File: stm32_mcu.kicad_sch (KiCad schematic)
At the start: 6 parts, among them J4 Conn_ARM_SWD_TagConnect_TC203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, U1 STM32G031J6Mx

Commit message: Update polygons
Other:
- moved on the sheet: J4
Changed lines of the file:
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@@
     (stroke (width 0) (type default))
   )
-  (wire (pts (xy 78.74 76.2) (xy 83.82 76.2))
+  (wire (pts (xy 267.97 76.2) (xy 273.05 76.2))
     (stroke (width 0) (type default))
   )
@@
     (stroke (width 0) (type default))
   )
-  (wire (pts (xy 78.74 81.28) (xy 83.82 81.28))
+  (wire (pts (xy 267.97 81.28) (xy 273.05 81.28))
     (stroke (width 0) (type default))
   )
@@
     (stroke (width 0) (type default))
   )
-  (wire (pts (xy 78.74 83.82) (xy 83.82 83.82))
+  (wire (pts (xy 267.97 83.82) (xy 273.05 83.82))
     (stroke (width 0) (type default))
   )
@@
     (stroke (width 0) (type default))
   )
-  (wire (pts (xy 68.58 91.44) (xy 68.58 92.71))
-    (stroke (width 0) (type default))
-  )
-  (wire (pts (xy 68.58 66.04) (xy 68.58 71.12))
+  (wire (pts (xy 257.81 91.44) (xy 257.81 92.71))
+    (stroke (width 0) (type default))
+  )
+  (wire (pts (xy 257.81 66.04) (xy 257.81 71.12))
     (stroke (width 0) (type default))
   )
@@
     )
   )
-  (global_label "JTMS" (shape input) (at 83.82 83.82 0)
-    (effects (font (size 1.27 1.27)) (justify left))
-    (property "Intersheetrefs" "${INTERSHEET_REFS}" (at 90.2334 83.82 0)
+  (global_label "JTMS" (shape input) (at 273.05 83.82 0)
+    (effects (font (size 1.27 1.27)) (justify left))
+    (property "Intersheetrefs" "${INTERSHEET_REFS}" (at 279.4634 83.82 0)
       (effects (font (size 1.27 1.27)) hide)
     )
@@
     )
   )
-  (global_label "JTCK" (shape input) (at 83.82 81.28 0)
-    (effects (font (size 1.27 1.27)) (justify left))
-    (property "Intersheetrefs" "${INTERSHEET_REFS}" (at 90.2334 81.28 0)
+  (global_label "JTCK" (shape input) (at 273.05 81.28 0)
+    (effects (font (size 1.27 1.27)) (justify left))
+    (property "Intersheetrefs" "${INTERSHEET_REFS}" (at 279.4634 81.28 0)
       (effects (font (size 1.27 1.27)) hide)
     )
@@
     )
   )
-  (global_label "JNRST" (shape input) (at 83.82 76.2 0)
-    (effects (font (size 1.27 1.27)) (justify left))
-    (property "Intersheetrefs" "${INTERSHEET_REFS}" (at 90.2334 76.2 0)
+  (global_label "JNRST" (shape input) (at 273.05 76.2 0)
+    (effects (font (size 1.27 1.27)) (justify left))
+    (property "Intersheetrefs" "${INTERSHEET_REFS}" (at 279.4634 76.2 0)
       (effects (font (size 1.27 1.27)) hide)
     )
@@
     )
   )
-  (symbol (lib_id "power:GND") (at 68.58 92.71 0) (unit 1)
-    (in_bom yes) (on_board yes) (dnp no)
-    (property "Reference" "#PWR09" (at 68.58 99.06 0)
-      (effects (font (size 1.27 1.27)) hide)
-    )
-    (property "Value" "GND" (at 68.707 97.1042 0)
-      (effects (font (size 1.27 1.27)))
-    )
-    (property "Footprint" "" (at 68.58 92.71 0)
-      (effects (font (size 1.27 1.27)) hide)
-    )
-    (property "Datasheet" "" (at 68.58 92.71 0)
+  (symbol (lib_id "power:GND") (at 257.81 92.71 0) (unit 1)
+    (in_bom yes) (on_board yes) (dnp no)
+    (property "Reference" "#PWR09" (at 257.81 99.06 0)
+      (effects (font (size 1.27 1.27)) hide)
+    )
+    (property "Value" "GND" (at 257.937 97.1042 0)
+      (effects (font (size 1.27 1.27)))
+    )
+    (property "Footprint" "" (at 257.81 92.71 0)
+      (effects (font (size 1.27 1.27)) hide)
+    )
+    (property "Datasheet" "" (at 257.81 92.71 0)
       (effects (font (size 1.27 1.27)) hide)
     )
@@
     )
   )
-  (symbol (lib_id "power:+5V") (at 68.58 66.04 0) (unit 1)
-    (in_bom yes) (on_board yes) (dnp no)
-    (property "Reference" "#PWR08" (at 68.58 69.85 0)
-      (effects (font (size 1.27 1.27)) hide)
-    )
-    (property "Value" "+5V" (at 68.961 61.6458 0)
-      (effects (font (size 1.27 1.27)))
-    )
-    (property "Footprint" "" (at 68.58 66.04 0)
-      (effects (font (size 1.27 1.27)) hide)
-    )
-    (property "Datasheet" "" (at 68.58 66.04 0)
+  (symbol (lib_id "power:+5V") (at 257.81 66.04 0) (unit 1)
+    (in_bom yes) (on_board yes) (dnp no)
+    (property "Reference" "#PWR08" (at 257.81 69.85 0)
+      (effects (font (size 1.27 1.27)) hide)
+    )
+    (property "Value" "+5V" (at 258.191 61.6458 0)
+      (effects (font (size 1.27 1.27)))
+    )
+    (property "Footprint" "" (at 257.81 66.04 0)
+      (effects (font (size 1.27 1.27)) hide)
+    )
+    (property "Datasheet" "" (at 257.81 66.04 0)
       (effects (font (size 1.27 1.27)) hide)
     )
@@
     )
   )
-  (symbol (lib_id "Connector:Conn_ARM_SWD_TagConnect_TC2030-NL") (at 71.12 81.28 0) (unit 1)
+  (symbol (lib_id "Connector:Conn_ARM_SWD_TagConnect_TC2030-NL") (at 260.35 81.28 0) (unit 1)
     (in_bom no) (on_board yes) (dnp no) (fields_autoplaced)
-    (property "Reference" "J4" (at 64.77 80.01 0)
+    (property "Reference" "J4" (at 254 80.01 0)
       (effects (font (size 1.27 1.27)) (justify right))
     )
-    (property "Value" "Conn_ARM_SWD_TagConnect_TC2030-NL" (at 64.77 82.55 0)
+    (property "Value" "Conn_ARM_SWD_TagConnect_TC2030-NL" (at 254 82.55 0)
       (effects (font (size 1.27 1.27)) (justify right))
     )
-    (property "Footprint" "Connector:Tag-Connect_TC2030-IDC-NL_2x03_P1.27mm_Vertical" (at 71.12 99.06 0)
-      (effects (font (size 1.27 1.27)) hide)
-    )
-    (property "Datasheet" "https://www.tag-connect.com/wp-content/uploads/bsk-pdf-manager/TC2030-CTX_1.pdf" (at 71.12 96.52 0)
-      (effects (font (size 1.27 1.27)) hide)
-    )
+    (property "Footprint" "Connector:Tag-Connect_TC2030-IDC-NL_2x03_P1.27mm_Vertical" (at 260.35 99.06 0)
+      (effects (font (size 1.27 1.27)) hide)
+    )
+    (property "Datasheet" "https://www.tag-connect.com/wp-content/uploads/bsk-pdf-manager/TC2030-CTX_1.pdf" (at 260.35 96.52 0)
+      (effects (font (size 1.27 1.27)) hide)
+    )

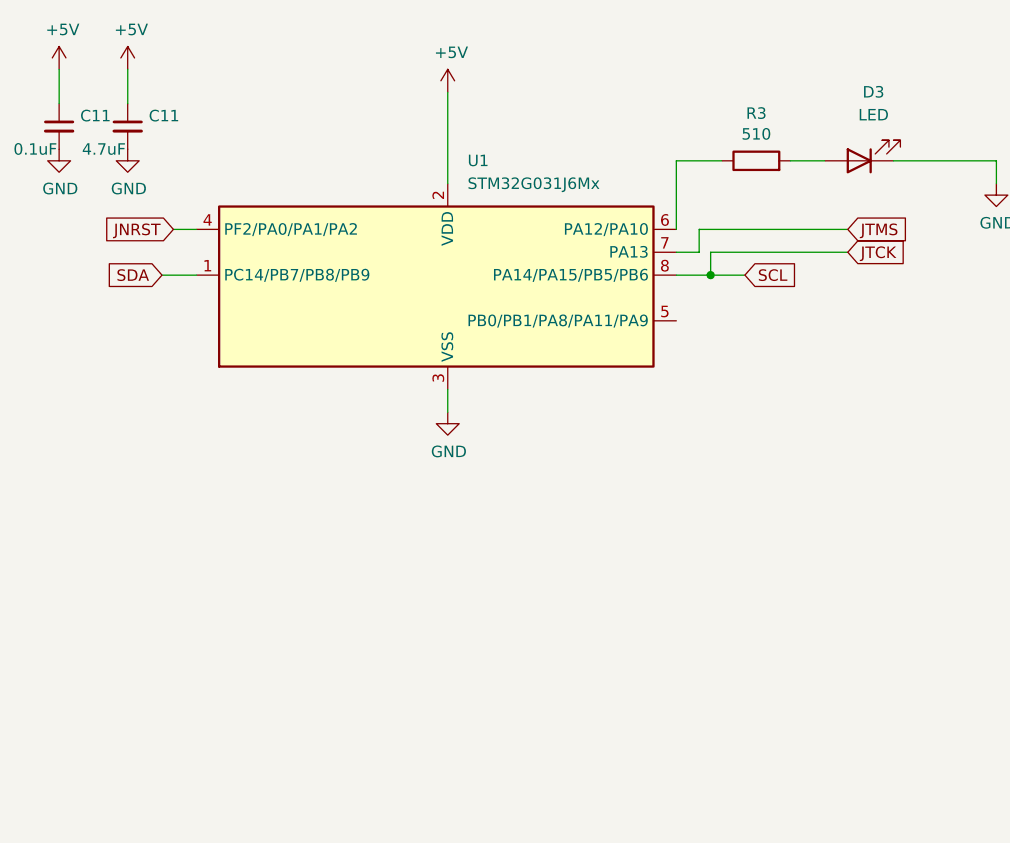
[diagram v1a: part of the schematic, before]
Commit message: Add proto area
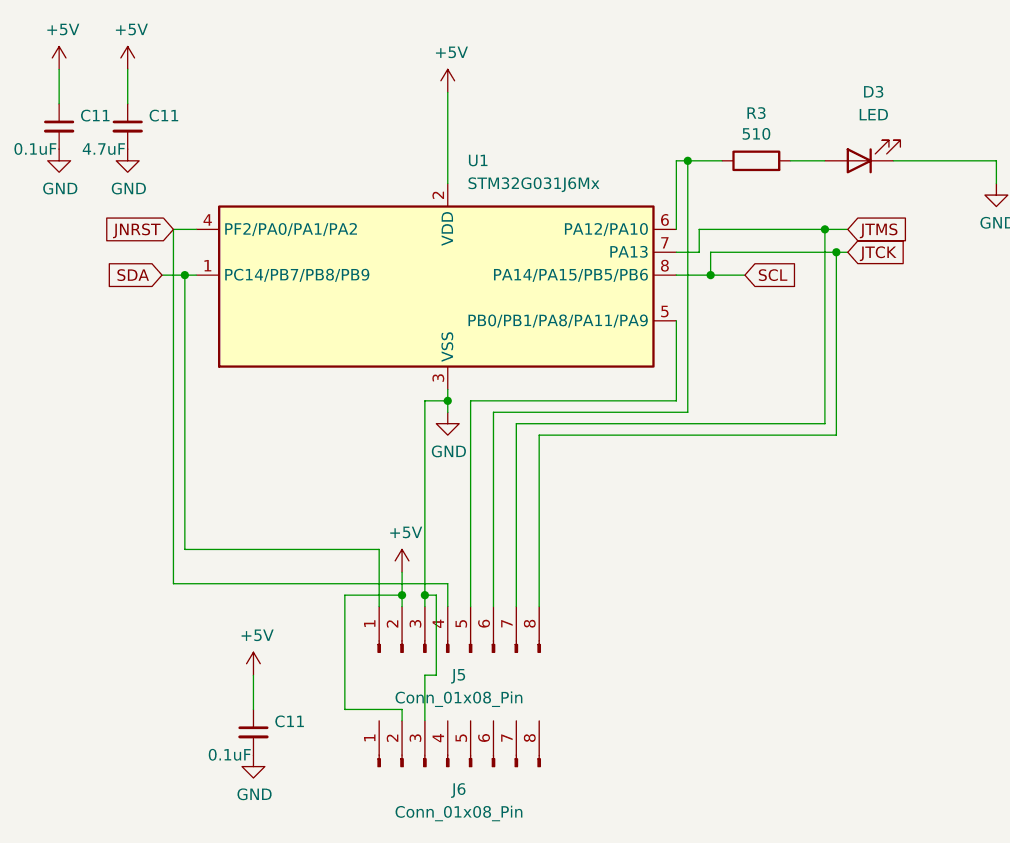
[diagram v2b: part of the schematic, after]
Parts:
- added C11: 0.1uF, Capacitor_SMD:C_0402_1005Metric, symbol Device:C_Small
- added J5, J6: Conn_01x08_Pin, Connector_PinHeader_1.00mm:PinHeader_1x08_P1.00mm_Vertical, symbol Connector:Conn_01x08_Pin
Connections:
- net +5V: now also C11.1, J5.2 (Pin_2), J6.2 (Pin_2)
- net GND: now also C11.2, J5.3 (Pin_3), J6.3 (Pin_3)
- net JNRST: now also J5.4 (Pin_4)
- net JTCK: now also J5.8 (Pin_8)
- net JTMS: now also J5.7 (Pin_7)
- net SDA: now also J5.1 (Pin_1)
- net at U1.5 (PB0/PB1/PA8/PA11/PA9): now also J5.5 (Pin_5)
- net at R3.1, U1.6 (PA12/PA10): now also J5.6 (Pin_6)

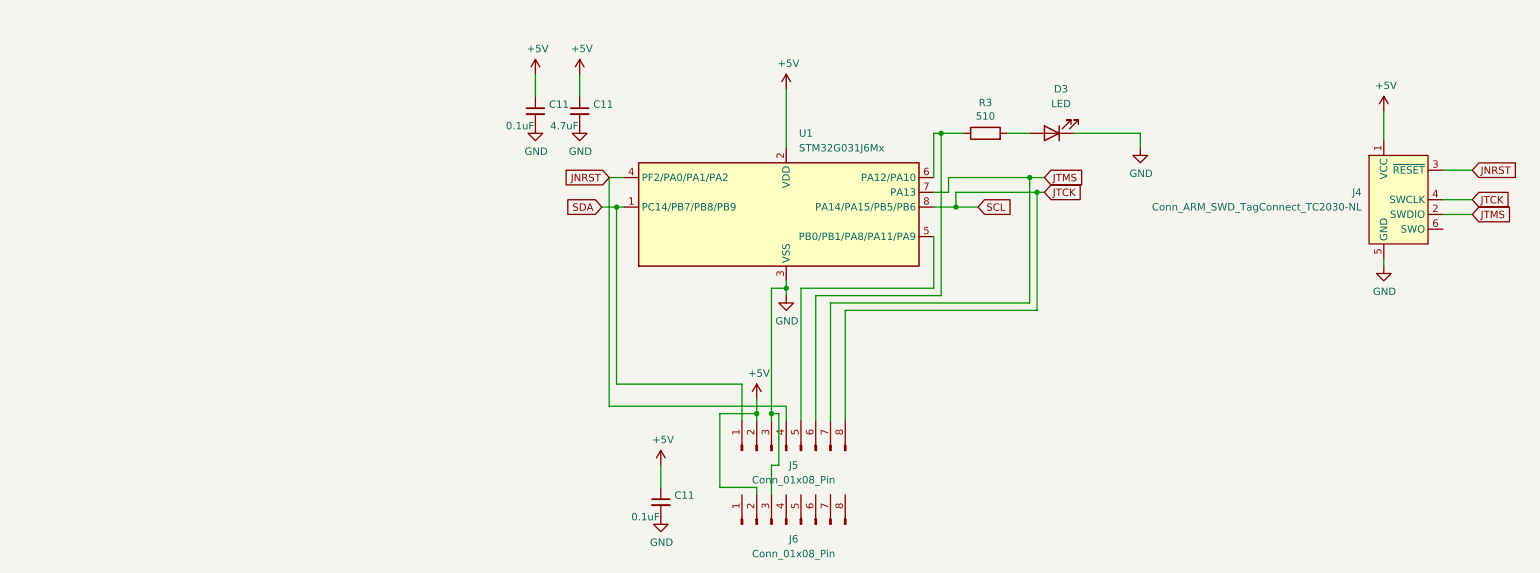
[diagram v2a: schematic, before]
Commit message: Add inductor
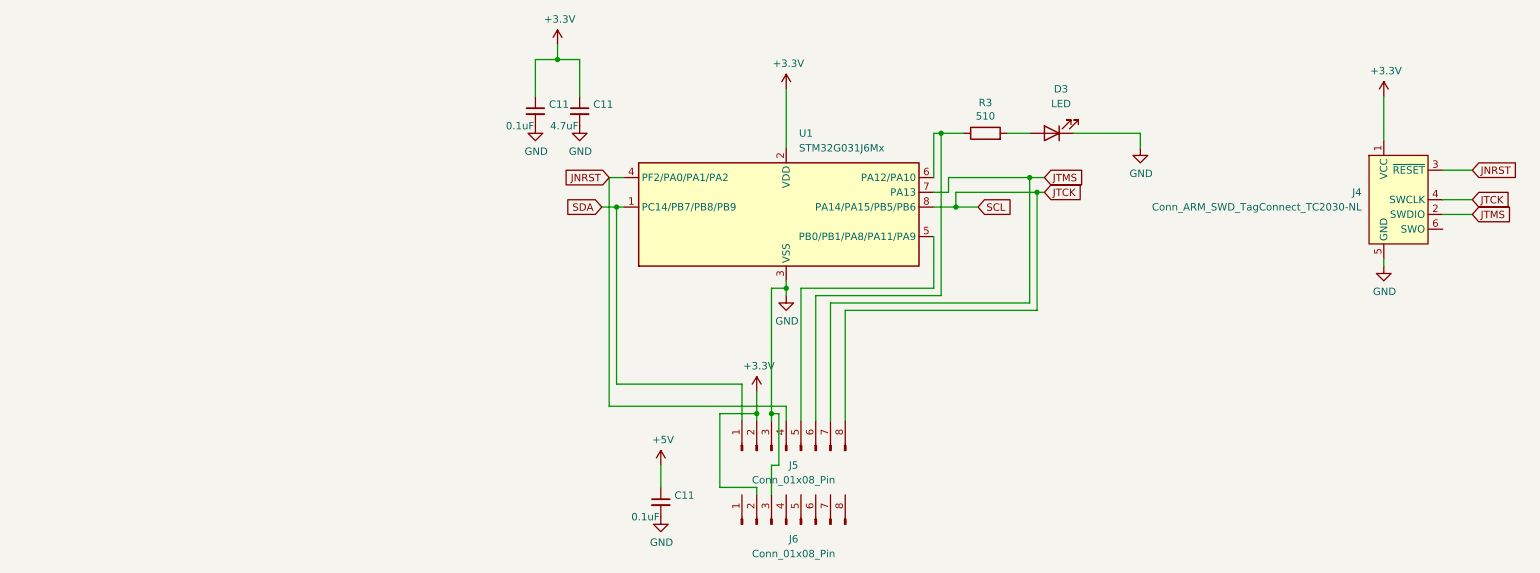
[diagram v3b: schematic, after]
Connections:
- net +5V: no longer C11.1, C11.1, J4.1 (VCC), J5.2 (Pin_2), J6.2 (Pin_2), U1.2 (VDD)
- new net +3V3: C11.1, C11.1, J4.1 (VCC), J5.2 (Pin_2), J6.2 (Pin_2), U1.2 (VDD)

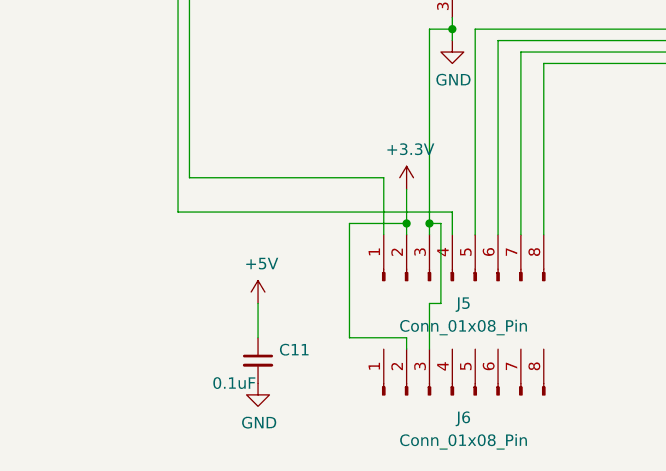
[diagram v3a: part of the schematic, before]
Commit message: Add dc-dc 3.3v to 5v
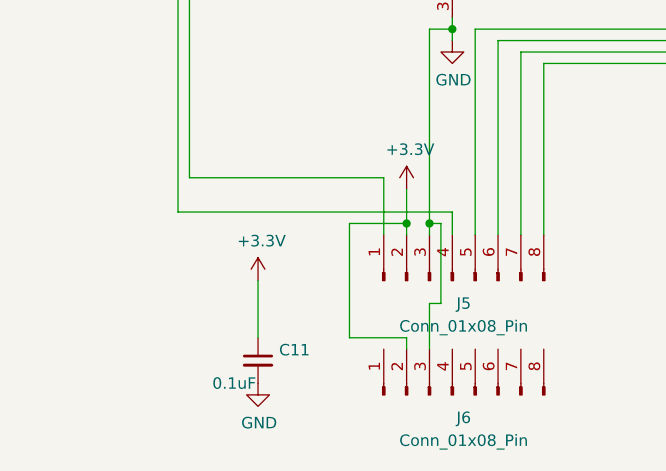
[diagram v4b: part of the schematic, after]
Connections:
- net +5V is gone; now on net +3V3: C11.1
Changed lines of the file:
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@@
     (stroke (width 0) (type default))
   )
-  (wire (pts (xy 133.35 127) (xy 133.35 130.81))
+  (wire (pts (xy 133.35 124.46) (xy 133.35 130.81))
     (stroke (width 0) (type default))
   )
@@
         (path "/eed35b77-cbf9-4596-9b17-2558f81058ba/c7f9496d-fb5e-4ce7-92b5-54c2d3a6681a"
           (reference "#PWR028") (unit 1)
+        )
+      )
+    )
+  )
+  (symbol (lib_id "rpi-pico-debugger-shoe-rescue:+3.3V-power") (at 133.35 124.46 0) (unit 1)
+    (in_bom yes) (on_board yes) (dnp no)
+    (property "Reference" "#PWR0104" (at 133.35 128.27 0)
+      (effects (font (size 1.27 1.27)) hide)
+    )
+    (property "Value" "+3.3V" (at 133.731 120.0658 0)
+      (effects (font (size 1.27 1.27)))
+    )
+    (property "Footprint" "" (at 133.35 124.46 0)
+      (effects (font (size 1.27 1.27)) hide)
+    )
+    (property "Datasheet" "" (at 133.35 124.46 0)
+      (effects (font (size 1.27 1.27)) hide)
+    )
+    (pin "1")
+    (instances
+      (project "rpi-pico-debugger-shoe"
+        (path "/aad74d97-f116-4a83-b498-c8cb2f4b4e35"
+          (reference "#PWR0104") (unit 1)
+        )
+      )
+      (project "ltp_kikad"
+        (path "/eed35b77-cbf9-4596-9b17-2558f81058ba"
+          (reference "#PWR0119") (unit 1)
+        )
+        (path "/eed35b77-cbf9-4596-9b17-2558f81058ba/c7f9496d-fb5e-4ce7-92b5-54c2d3a6681a"
+          (reference "#PWR030") (unit 1)
         )
       )
@@
         )
       )
-    )
-  )
-  (symbol (lib_id "power:+5V") (at 133.35 127 0) (unit 1)
-    (in_bom yes) (on_board yes) (dnp no)
-    (property "Reference" "#PWR08" (at 133.35 130.81 0)
-      (effects (font (size 1.27 1.27)) hide)
-    )
-    (property "Value" "+5V" (at 133.731 122.6058 0)
-      (effects (font (size 1.27 1.27)))
-    )
-    (property "Footprint" "" (at 133.35 127 0)
-      (effects (font (size 1.27 1.27)) hide)
-    )
-    (property "Datasheet" "" (at 133.35 127 0)
-      (effects (font (size 1.27 1.27)) hide)
-    )
-    (pin "1")
-    (instances
-      (project "LTP305_ESP32_CLOCK"
-        (path "/c007e288-8439-49d9-bbdf-49724c34958c"
-          (reference "#PWR08") (unit 1)
-        )
-      )
-      (project "ltp_kikad"
-        (path "/eed35b77-cbf9-4596-9b17-2558f81058ba"
-          (reference "#PWR04") (unit 1)
-        )
-        (path "/eed35b77-cbf9-4596-9b17-2558f81058ba/7d22e16e-a0ba-4766-b1de-c8cbb28f14f7"
-          (reference "#PWR020") (unit 1)
-        )
-        (path "/eed35b77-cbf9-4596-9b17-2558f81058ba/c7f9496d-fb5e-4ce7-92b5-54c2d3a6681a"
-          (reference "#PWR039") (unit 1)
-        )
-      )
